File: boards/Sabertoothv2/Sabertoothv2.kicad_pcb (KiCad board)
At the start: 2 copper layers, 45.6 x 45.6 mm, 40 parts, among them J1 Screw_Terminal_01x04, J2 Screw_Terminal_01x04, J4 Conn_01x04_Pin, J5 Conn_01x04_Pin, Q1 NMOS, Q2 NMOS, Q3 NMOS, Q4 NMOS, U1 LM2104, U2 LM2104, U4 74LVC1GU04DRL

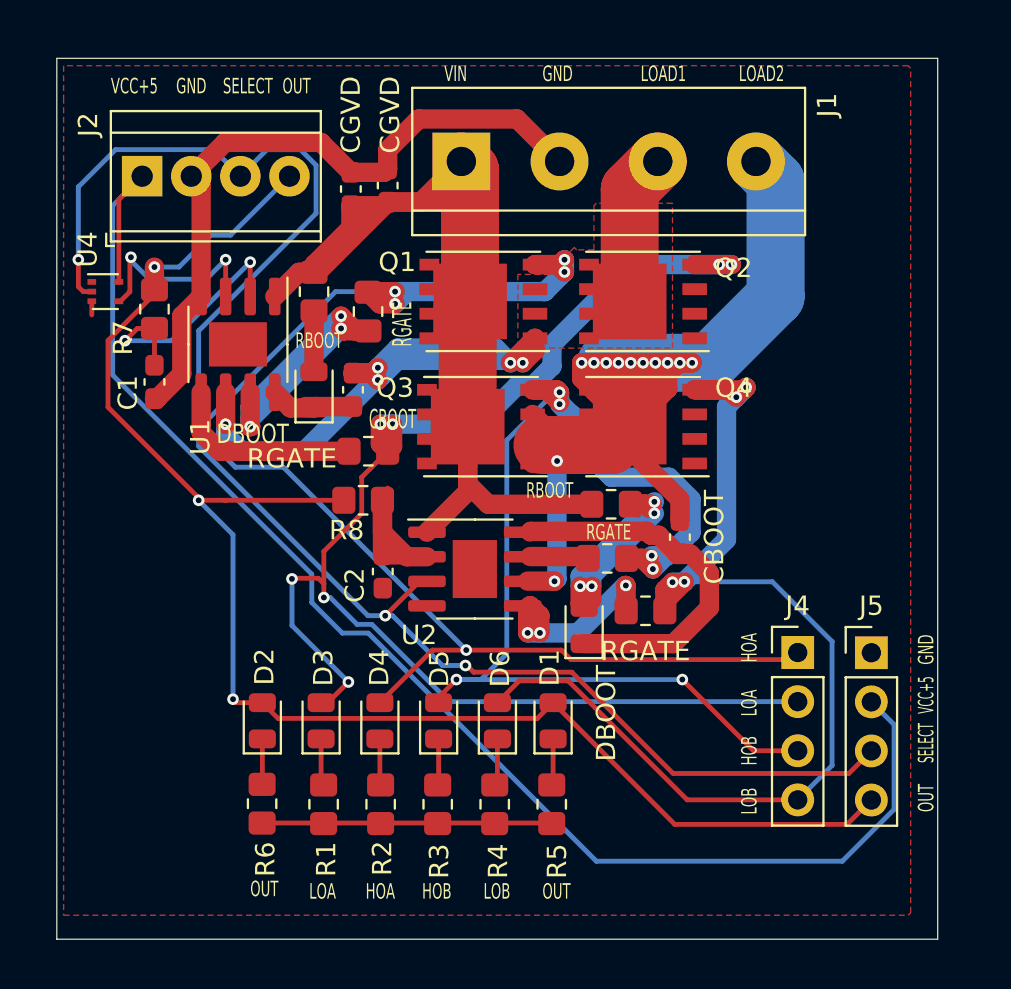
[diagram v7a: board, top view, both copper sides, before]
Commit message: minor correction for the filling zone
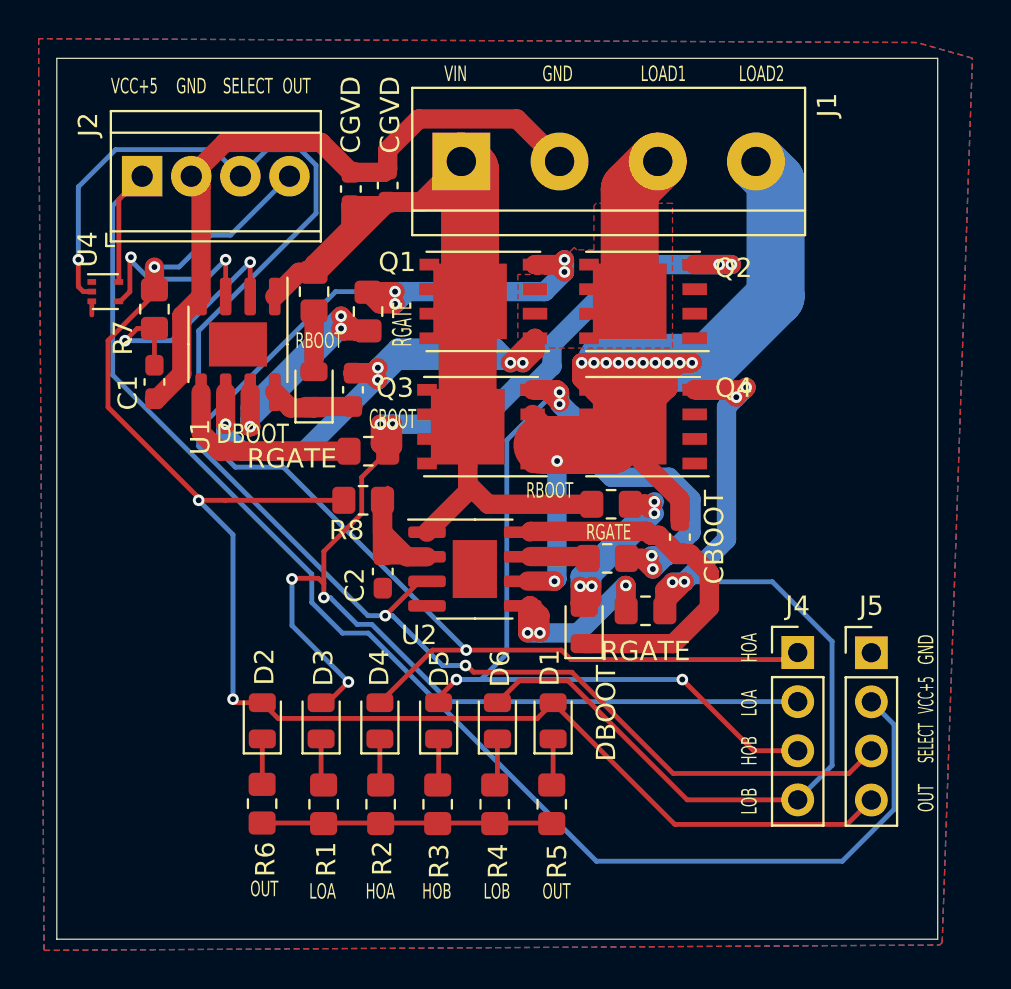
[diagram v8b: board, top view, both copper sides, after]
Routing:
- added copper zone on B.Cu, net GND
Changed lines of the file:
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@@
   (segment (start 54.6645 30.607) (end 54.6645 30.783384) (width 0.25) (layer "B.Cu") (net 28))
   (segment (start 54.6645 30.783384) (end 55.621116 31.74) (width 0.25) (layer "B.Cu") (net 28))
-  (zone (net 2) (net_name "GND") (layer "F.Cu") (hatch edge 0.5)
-    (connect_pads (clearance 0.5))
-    (min_thickness 0.25) (filled_areas_thickness no)
-    (fill yes (thermal_gap 0) (thermal_bridge_width 3))
-    (polygon
-      (pts
-        (xy 51.181 64.643)
-        (xy 94.869 64.643)
-        (xy 94.996 64.516)
-        (xy 94.996 20.828)
-        (xy 94.869 20.701)
-        (xy 51.181 20.701)
-        (xy 51.181 22.352)
-      )
-    )
-  )
   (zone (net 20) (net_name "LOAD1") (layer "F.Cu") (hatch edge 0.5)
     (priority 1)
@@
       )
     )
+  )
+  (zone (net 2) (net_name "GND") (layers "F&B.Cu") (hatch edge 0.5)
+    (connect_pads (clearance 0.5))
+    (min_thickness 0.25) (filled_areas_thickness no)
+    (fill yes (thermal_gap 0) (thermal_bridge_width 3))
+    (polygon
+      (pts
+        (xy 50.17 66.46)
+        (xy 96.499 66.183)
+        (xy 96.626 66.056)
+        (xy 98.19 20.31)
+        (xy 95.319 19.501)
+        (xy 49.891 19.301)
+        (xy 49.891 20.952)
+      )
+    )
